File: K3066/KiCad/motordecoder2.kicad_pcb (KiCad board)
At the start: 2 copper layers, 60 x 10.5 mm, 73 parts, among them J11 PAD, J12 PAD, J14 PAD, J16 PAD, J18 PAD, J19 PAD, P1 PAD, P10 PAD, P11 PAD, P2 PAD, P3 PAD, P4 PAD, P5 PAD, P6 PAD, P7 PAD, P8 PAD, P9 PROG, Q1 DMG6601LVT, Q11 SSM3K7002BFU, Q12 SSM6N7002BFE, Q13 SSM6N7002BFE, Q14 SSM6N7002BFE, Q2 DMG6601LVT, Q21 PMBT3906VS, Q22 SSM6N7002BFE, Q3 PMBT3904VS, Q5 2SC4116, Q6 PMBT3906VS, Q8 PMBT3904VS, U2 ATtiny1606-M

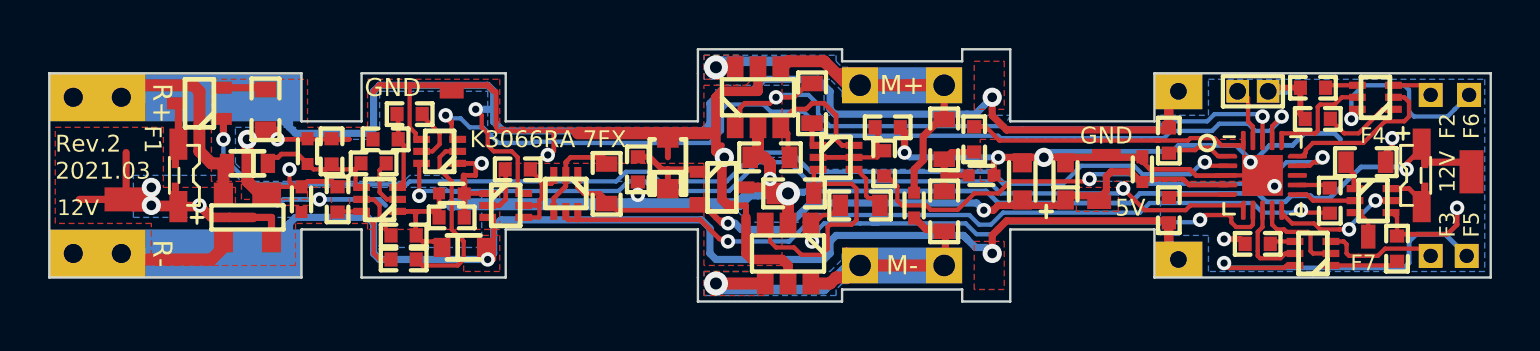
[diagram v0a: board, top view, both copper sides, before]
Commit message: 回路の問題点を修正 (K3066: Rev3 / それ以外: Rev2)
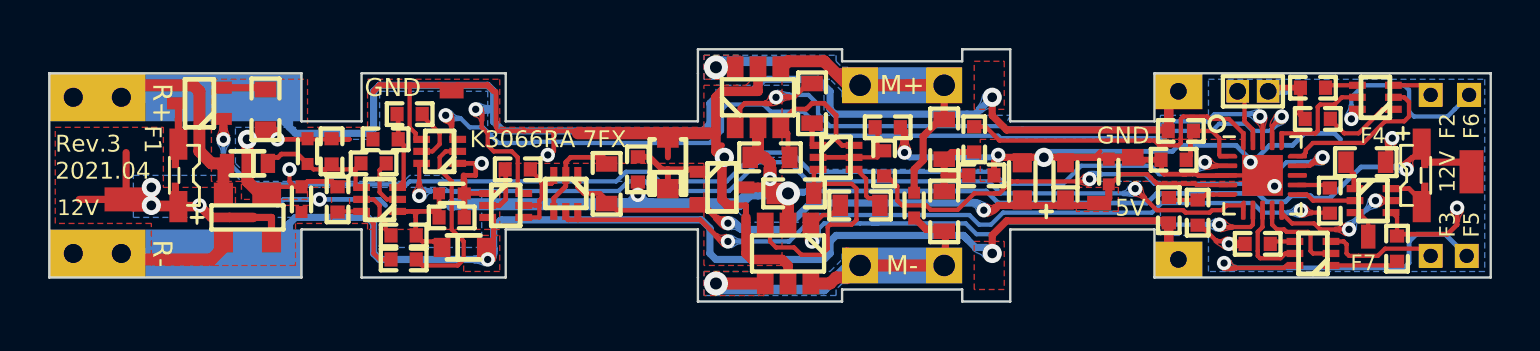
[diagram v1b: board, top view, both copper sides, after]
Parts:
- removed C6: 104, footprint:C_1005_v2
- added R16: 103, footprint:R_1005, F.Cu at (156.8, 100.8)
- added R17: 104, footprint:R_1005, F.Cu at (164.8, 100.1)
- added R18: 104, footprint:R_1005, F.Cu at (165.8, 102.3)
- C7: value 104 -> 182
- D3: value UDZV5.1B -> UDZV5.6B
- P11: footprint footprint:PAD_0.5x1.2_SMD -> footprint:PAD_0.7x0.9_SMD
- R23, R24, R25, R26: value 102 -> 472
- moved C5 1.40 mm to (162.1, 100.6)
- moved P11 1.10 mm to (163.1, 100.0)
- moved R1 0.64 mm to (165.1, 98.9), turned to 0 degrees
- moved P10 0.05 mm to (161.7, 101.9)
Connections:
- net Func8 renamed DIR_JP
- Q12 pad 2: Func2 -> Func4
- Q13 pad 2: Func3 -> Func5
- Q13 pad 5: Func4 -> Func3
- Q14 pad 2: Func5 -> Func6
- Q14 pad 5: Func6 -> Func2
- U2 pad 11: Func2 -> Func4
- U2 pad 15: Func5 -> Func6
- U2 pad 16: Func6 -> Func2
- U2 pad 8: Func4 -> Func3
- U2 pad 9: Func3 -> Func5
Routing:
- net Func5: track 6.72 -> 3.96 mm
- net Func2: track 2.50 -> 4.66 mm
- net Func6: track 4.66 -> 6.72 mm
- net GND: track 94.1 -> 95.9 mm
- net +12V: track 77.7 -> 79.1 mm
- net BEMF: track 12.0 -> 13.3 mm
- net Func4: track 3.66 -> 2.50 mm
- net Net-(R1-Pad2): track 2.69 -> 3.72 mm
- net FWD: track 23.7 -> 22.9 mm
- net +5V: track 32.5 -> 33.1 mm
- net Func1: track 46.0 -> 46.5 mm
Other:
- board text added: "Rev.3 2021.04"
- board text removed: "Rev.2 2021.03"

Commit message: 基板上のF表記をP表記に変更
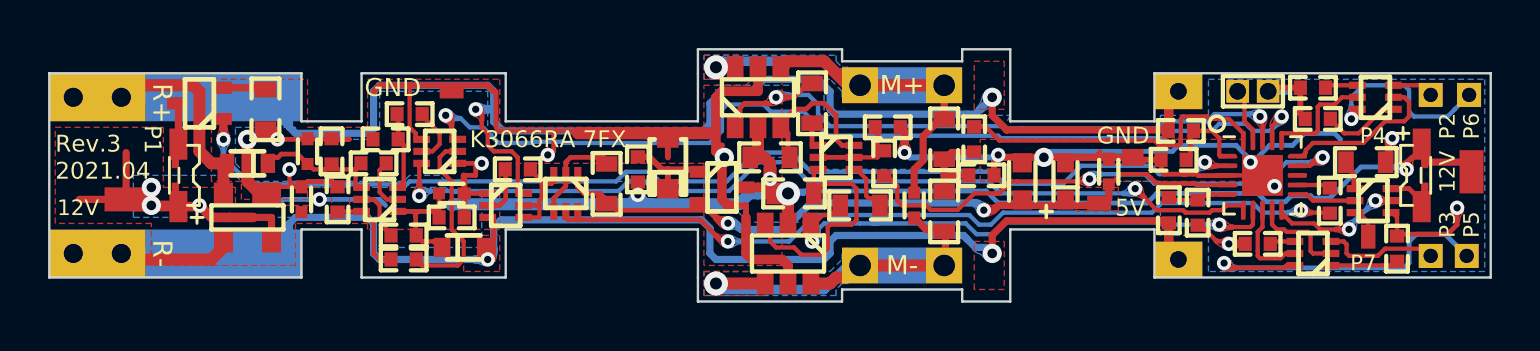
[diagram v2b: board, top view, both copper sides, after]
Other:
- board text added: "P1"
- board text added: "P2"
- board text added: "P3"
- board text added: "P4"
- board text added: "P5"
- board text added: "P6"
- board text added: "P7"
- board text removed: "F1"
- board text removed: "F2"
- board text removed: "F3"
- board text removed: "F4"
- board text removed: "F5"
- board text removed: "F6"
- board text removed: "F7"
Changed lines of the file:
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@@
   (gr_line (start 159.25 102.25) (end 159.75 102.25) (layer F.SilkS) (width 0.15))
   (gr_circle (center 166.6 98.6) (end 166.9 98.7) (layer F.SilkS) (width 0.15))
-  (gr_text F7 (at 172.7 104.4) (layer F.SilkS)
+  (gr_text P7 (at 172.7 104.4) (layer F.SilkS)
     (effects (font (size 0.65 0.65) (thickness 0.15)))
   )
-  (gr_text F4 (at 173.1 99.1) (layer F.SilkS)
+  (gr_text P4 (at 173.1 99.1) (layer F.SilkS)
     (effects (font (size 0.65 0.65) (thickness 0.15)))
   )
-  (gr_text F5 (at 177.2 102.8 90) (layer F.SilkS)
+  (gr_text P5 (at 177.2 102.8 90) (layer F.SilkS)
     (effects (font (size 0.65 0.65) (thickness 0.15)))
   )
-  (gr_text F3 (at 176.2 102.8 90) (layer F.SilkS)
+  (gr_text P3 (at 176.2 102.8 90) (layer F.SilkS)
     (effects (font (size 0.65 0.65) (thickness 0.15)))
   )
-  (gr_text F6 (at 177.2 98.7 90) (layer F.SilkS)
+  (gr_text P6 (at 177.2 98.7 90) (layer F.SilkS)
     (effects (font (size 0.65 0.65) (thickness 0.15)))
   )
-  (gr_text F2 (at 176.2 98.7 90) (layer F.SilkS)
+  (gr_text P2 (at 176.2 98.7 90) (layer F.SilkS)
     (effects (font (size 0.65 0.65) (thickness 0.15)))
   )
@@
     (effects (font (size 0.8 0.8) (thickness 0.2)))
   )
-  (gr_text F1 (at 122.3 99.25 -90) (layer F.SilkS)
+  (gr_text P1 (at 122.3 99.25 -90) (layer F.SilkS)
     (effects (font (size 0.7 0.7) (thickness 0.15)))
   )
